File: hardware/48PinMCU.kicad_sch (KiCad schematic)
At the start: 34 parts, among them J1 SWD_Header, J2 SWD, SW1 Reset, SW2 SW_SPDT, U1 STM32G473CETx, Y1 Crystal

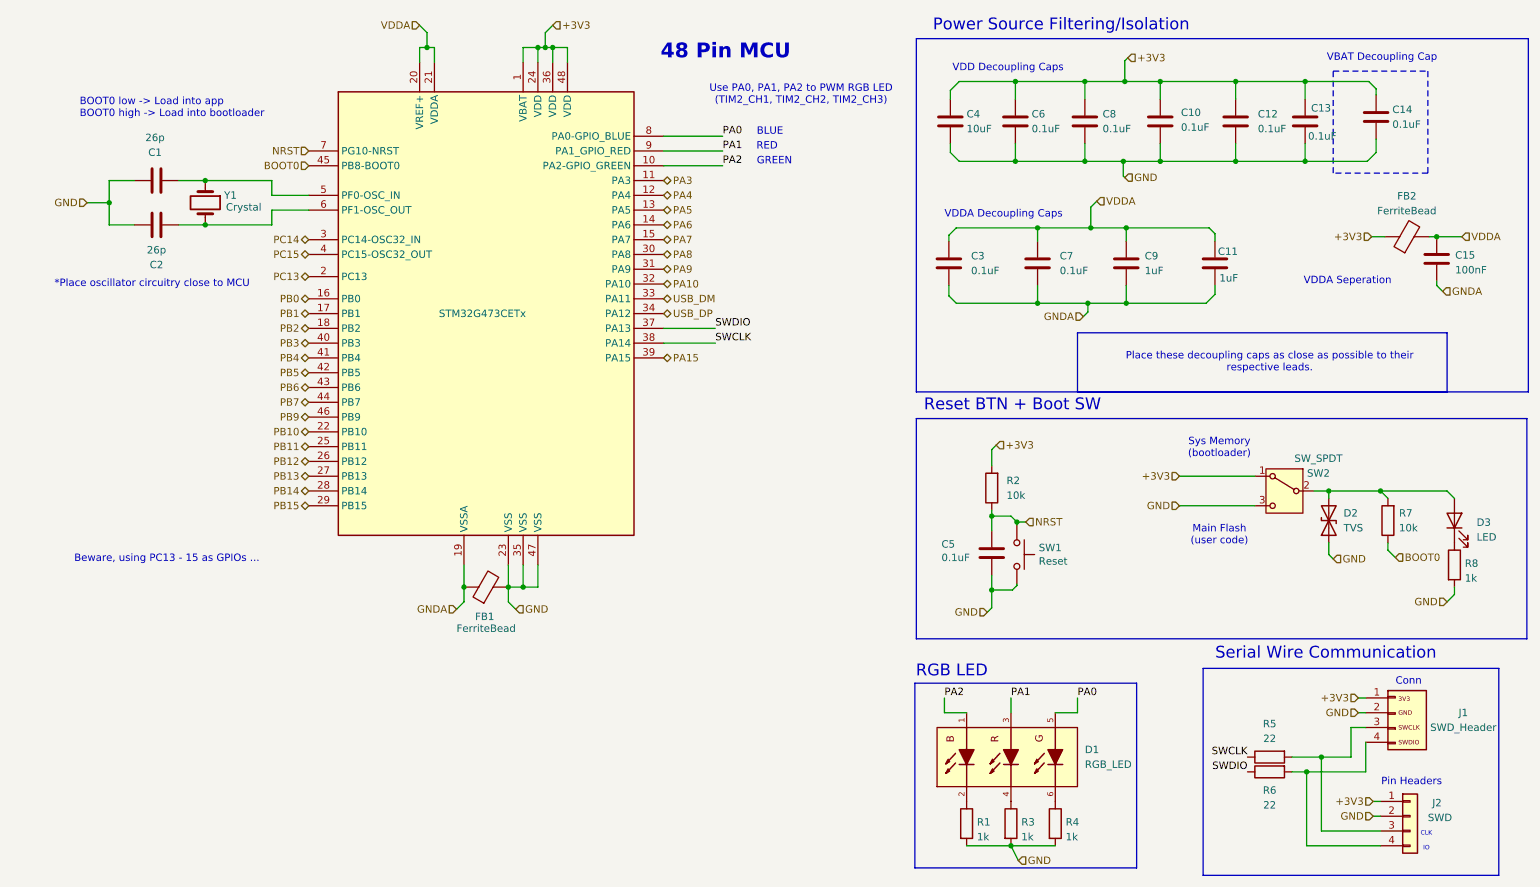
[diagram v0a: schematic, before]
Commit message: Fixed ERC
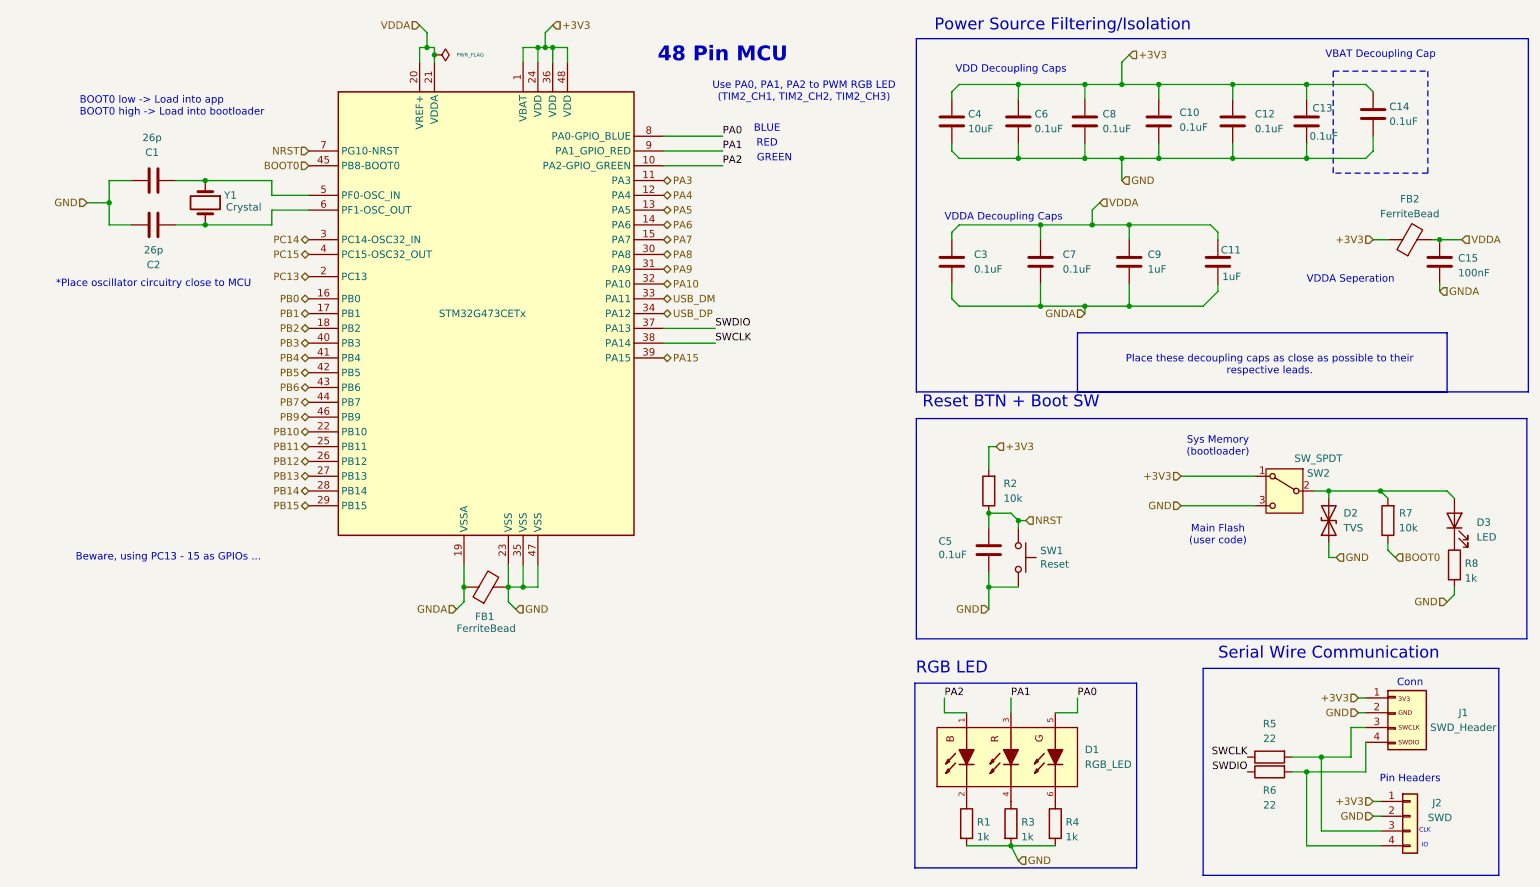
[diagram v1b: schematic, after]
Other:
- moved on the sheet: C1, C11, C12, C14, C15, C2, C3, C5, C6, C7, C9, FB2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

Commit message: ELC review changes implemented
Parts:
- added C47: 10uF, Capacitor_SMD:C_0603_1608Metric_Pad1.08x0.95mm_HandSolder, symbol Device:C
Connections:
- net GNDA: now also C47.2
- net VDDA: now also C47.1
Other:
- note added: "What do I do now thatr i have 4 channels thins kinda means 40mA all flow thorugh the ferrite bead can you explain what to do?"
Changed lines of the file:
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@@
 		)
 	)
+	(text "What do I do now thatr i have 4 channels thins kinda means  40mA all flow thorugh the ferrite bead can you explain what to do?"
+		(exclude_from_sim no)
+		(at 96.266 126.238 0)
+		(effects
+			(font
+				(size 1.27 1.27)
+			)
+		)
+	)
 	(text "RED"
 		(exclude_from_sim no)
@@
 	)
 	(junction
+		(at 214.63 66.04)
+		(diameter 0)
+		(color 0 0 0 0)
+	)
+	(junction
 		(at 102.87 21.59)
 		(diameter 0)
@@
 	)
 	(junction
+		(at 215.9 52.07)
+		(diameter 0)
+		(color 0 0 0 0)
+	)
+	(junction
 		(at 182.88 102.87)
 		(diameter 0)
@@
 	(wire
 		(pts
+			(xy 226.06 62.23) (xy 226.06 66.04)
+		)
+		(stroke
+			(width 0)
+			(type default)
+		)
+	)
+	(wire
+		(pts
 			(xy 132.08 41.91) (xy 121.92 41.91)
 		)
@@
 	(wire
 		(pts
+			(xy 226.06 66.04) (xy 214.63 66.04)
+		)
+		(stroke
+			(width 0)
+			(type default)
+		)
+	)
+	(wire
+		(pts
 			(xy 243.84 54.61) (xy 246.38 54.61)
 		)
@@
 	(wire
 		(pts
+			(xy 226.06 52.07) (xy 226.06 54.61)
+		)
+		(stroke
+			(width 0)
+			(type default)
+		)
+	)
+	(wire
+		(pts
 			(xy 80.01 21.59) (xy 81.28 21.59)
 		)
@@
 	(wire
 		(pts
+			(xy 215.9 52.07) (xy 226.06 52.07)
+		)
+		(stroke
+			(width 0)
+			(type default)
+		)
+	)
+	(wire
+		(pts
 			(xy 26.67 52.07) (xy 30.48 52.07)
 		)
@@
 					(unit 1)
 				)
+			)
+		)
+	)
+	(symbol
+		(lib_id "Device:C")
+		(at 226.06 58.42 0)
+		(unit 1)
+		(body_style 1)
+		(exclude_from_sim no)
+		(in_bom yes)
+		(on_board yes)
+		(in_pos_files yes)
+		(dnp no)
+		(property "Reference" "C47"
+			(at 226.568 56.388 0)
+			(show_name no)
+			(do_not_autoplace no)
+			(effects
+				(font
+					(size 1.27 1.27)
+				)
+				(justify left)
+			)
+		)
+		(property "Value" "10uF"
+			(at 226.822 60.96 0)
+			(show_name no)
+			(do_not_autoplace no)
+			(effects
+				(font
+					(size 1.27 1.27)
+				)
+				(justify left)
+			)
+		)
+		(property "Footprint" "Capacitor_SMD:C_0603_1608Metric_Pad1.08x0.95mm_HandSolder"
+			(at 227.0252 62.23 0)
+			(hide yes)
+			(show_name no)
+			(do_not_autoplace no)
+			(effects
+				(font
+					(size 1.27 1.27)
+				)
+			)
+		)
+		(property "Datasheet" ""
+			(at 226.06 58.42 0)
+			(hide yes)
+			(show_name no)
+			(do_not_autoplace no)
+			(effects
+				(font
+					(size 1.27 1.27)
+				)
+			)
+		)
+		(property "Description" "Unpolarized capacitor"
+			(at 226.06 58.42 0)
+			(hide yes)
+			(show_name no)
+			(do_not_autoplace no)
+			(effects
+				(font
+					(size 1.27 1.27)
+				)
+			)
+		)
+		(property "Mouser Part Number" "MLASH168SB7104KTNA01"
+			(at 226.06 58.42 0)
+			(hide yes)
+			(show_name no)
+			(do_not_autoplace no)
+			(effects
+				(font
+					(size 1.27 1.27)
+				)
+			)
+		)
+		(property "P/N" "MLASU168SB5105KTNA01"
+			(at 226.06 58.42 0)
+			(hide yes)
+			(show_name no)
+			(do_not_autoplace no)
+			(effects
+				(font
+					(size 1.27 1.27)
+				)
+			)
+		)
+		(property "Color" ""
+			(at 226.06 58.42 0)
+			(show_name no)
+			(do_not_autoplace no)
+			(effects
+				(font
+					(size 1.27 1.27)
+				)
+			)
+		)
+		(property "If" ""
+			(at 226.06 58.42 0)
+			(show_name no)
+			(do_not_autoplace no)
+			(effects
+				(font
+					(size 1.27 1.27)
+				)
+			)
+		)
+		(property "Mfg" ""
+			(at 226.06 58.42 0)
+			(show_name no)
+			(do_not_autoplace no)
+			(effects
+				(font
+					(size 1.27 1.27)
+				)
+			)
+		)
+		(property "Vf" ""
+			(at 226.06 58.42 0)
+			(show_name no)
+			(do_not_autoplace no)
+			(effects
+				(font
+					(size 1.27 1.27)
+				)
+			)
+		)
+		(property "LCSC P/N" "C15849"
+			(at 226.06 58.42 0)
+			(hide yes)
+			(show_name no)
+			(do_not_autoplace no)
+			(effects
+				(font
+					(size 1.27 1.27)
+				)
+			)
+		)
+		(pin "1"
+		)
+		(pin "2"
+		)
+		(instances
+			(project "StrainGaugeBoard"
+				(path "/fb459b39-605b-4b65-b2c9-e248812f4f03/cc54fbd4-47b5-4c2e-a438-64ef2059228d"
+					(reference "C47")
+					(unit 1)
+				)

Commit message: errors fixed
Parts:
- C19: renamed from C4; value 10uF -> 10u
- C24: renamed from C3; value 0.1uF -> 0.1u
- C37: renamed from C5; value 0.1uF -> 0.1u
- C38: renamed from C6; value 0.1uF -> 0.1u
- C39: renamed from C7; value 0.1uF -> 0.1u
- C59: renamed from C8; value 0.1uF -> 0.1u
- C63: renamed from C9; value 1uF -> 1u
- C64: renamed from C10; value 0.1uF -> 0.1u
- C65: renamed from C11; value 1uF -> 1u
- C69: renamed from C12; value 0.1uF -> 0.1u
- C71: renamed from C47; value 10uF -> 10u; footprint Capacitor_SMD:C_0603_1608Metric_Pad1.08x0.95mm_HandSolder -> Capacitor_SMD:C_0805_2012Metric_Pad1.18x1.45mm_HandSolder; LCSC P/N C15849 -> C440198; P/N MLASU168SB5105KTNA01 -> GRM21BR61H106KE43L
- C73: renamed from C13; value 0.1uF -> 0.1u
- C76: renamed from C14; value 0.1uF -> 0.1u
- C77: renamed from C15; value 100nF -> 100n; LCSC P/N C15849 -> C14663
- renumbered C1 to C17, C2 to C18, D3 to D18, D1 to D7, D2 to D8, FB1 to FB3, FB2 to FB4, J1 to J3, J2 to J9, R1 to R11, R2 to R12, R3 to R18, R4 to R19, R5 to R20, R6 to R21, R7 to R57, R8 to R58, SW1 to SW3, SW2 to SW4, U1 to U2, Y1 to Y2
